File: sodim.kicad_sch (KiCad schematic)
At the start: 1 part, among them J1 ddr4-sodimm-edge-connector

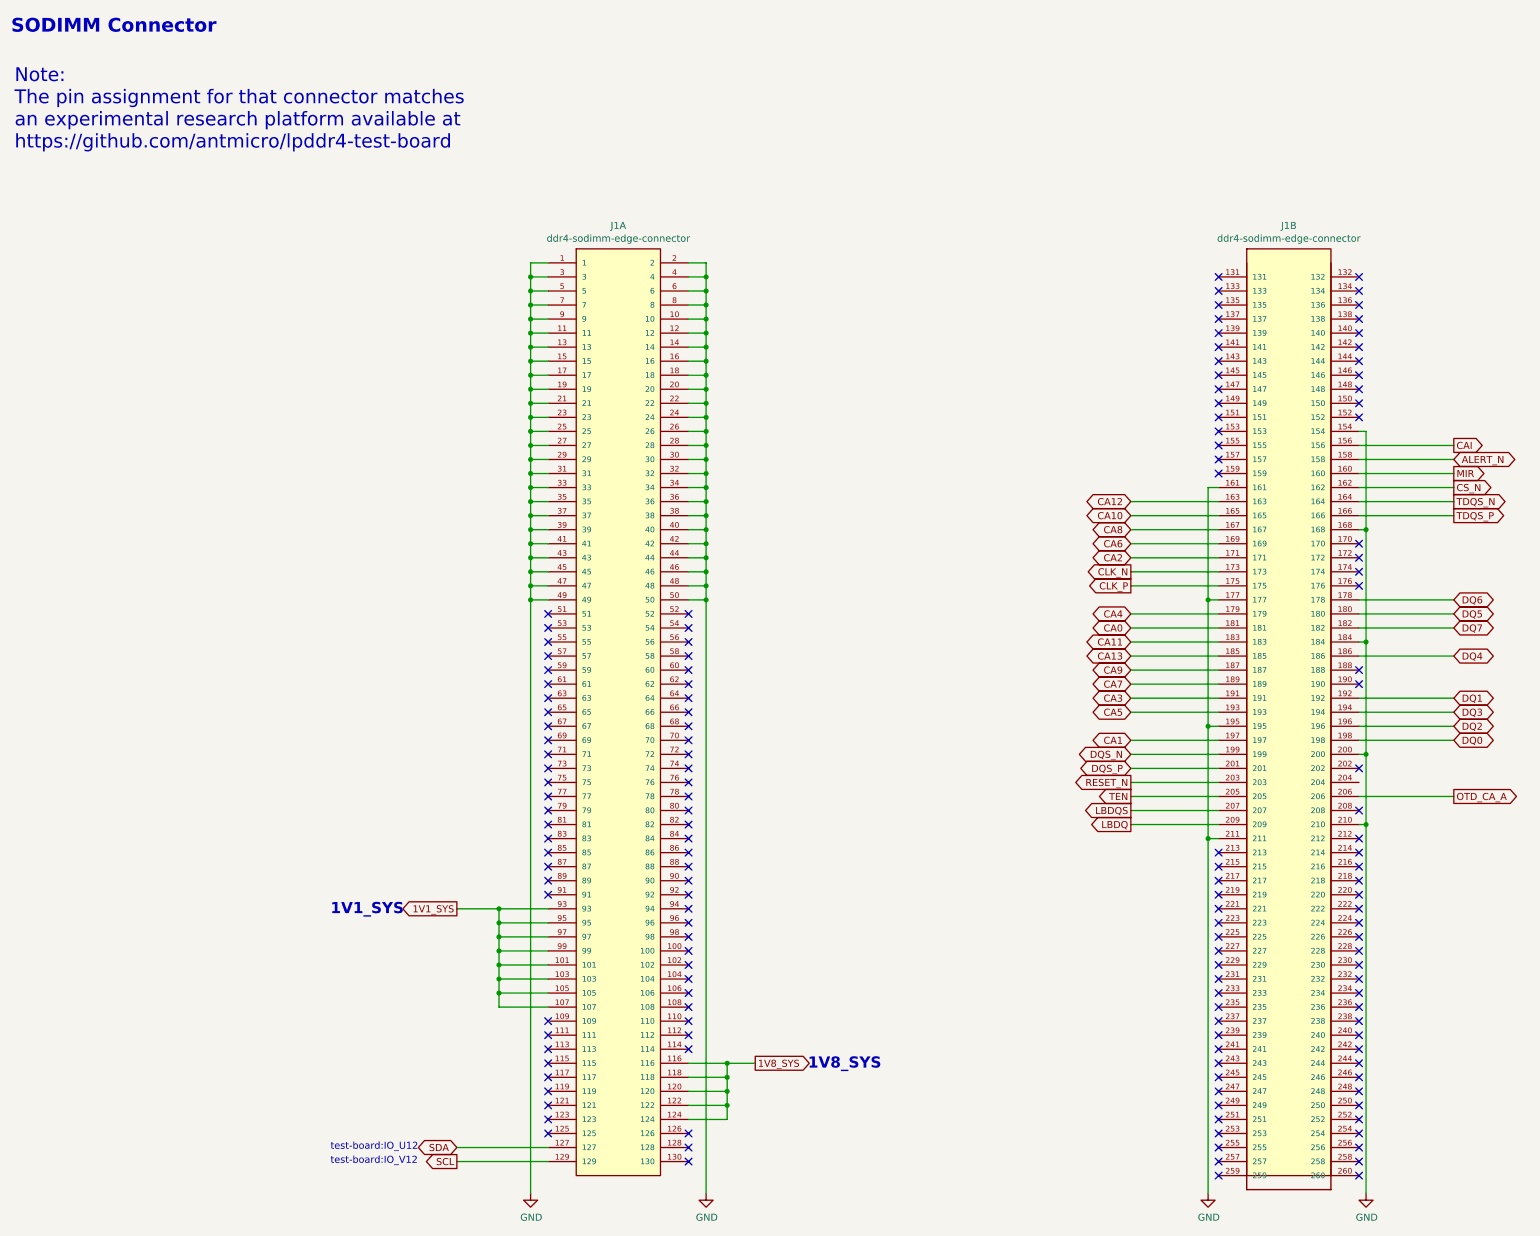
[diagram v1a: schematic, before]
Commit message: Introduce component standardization
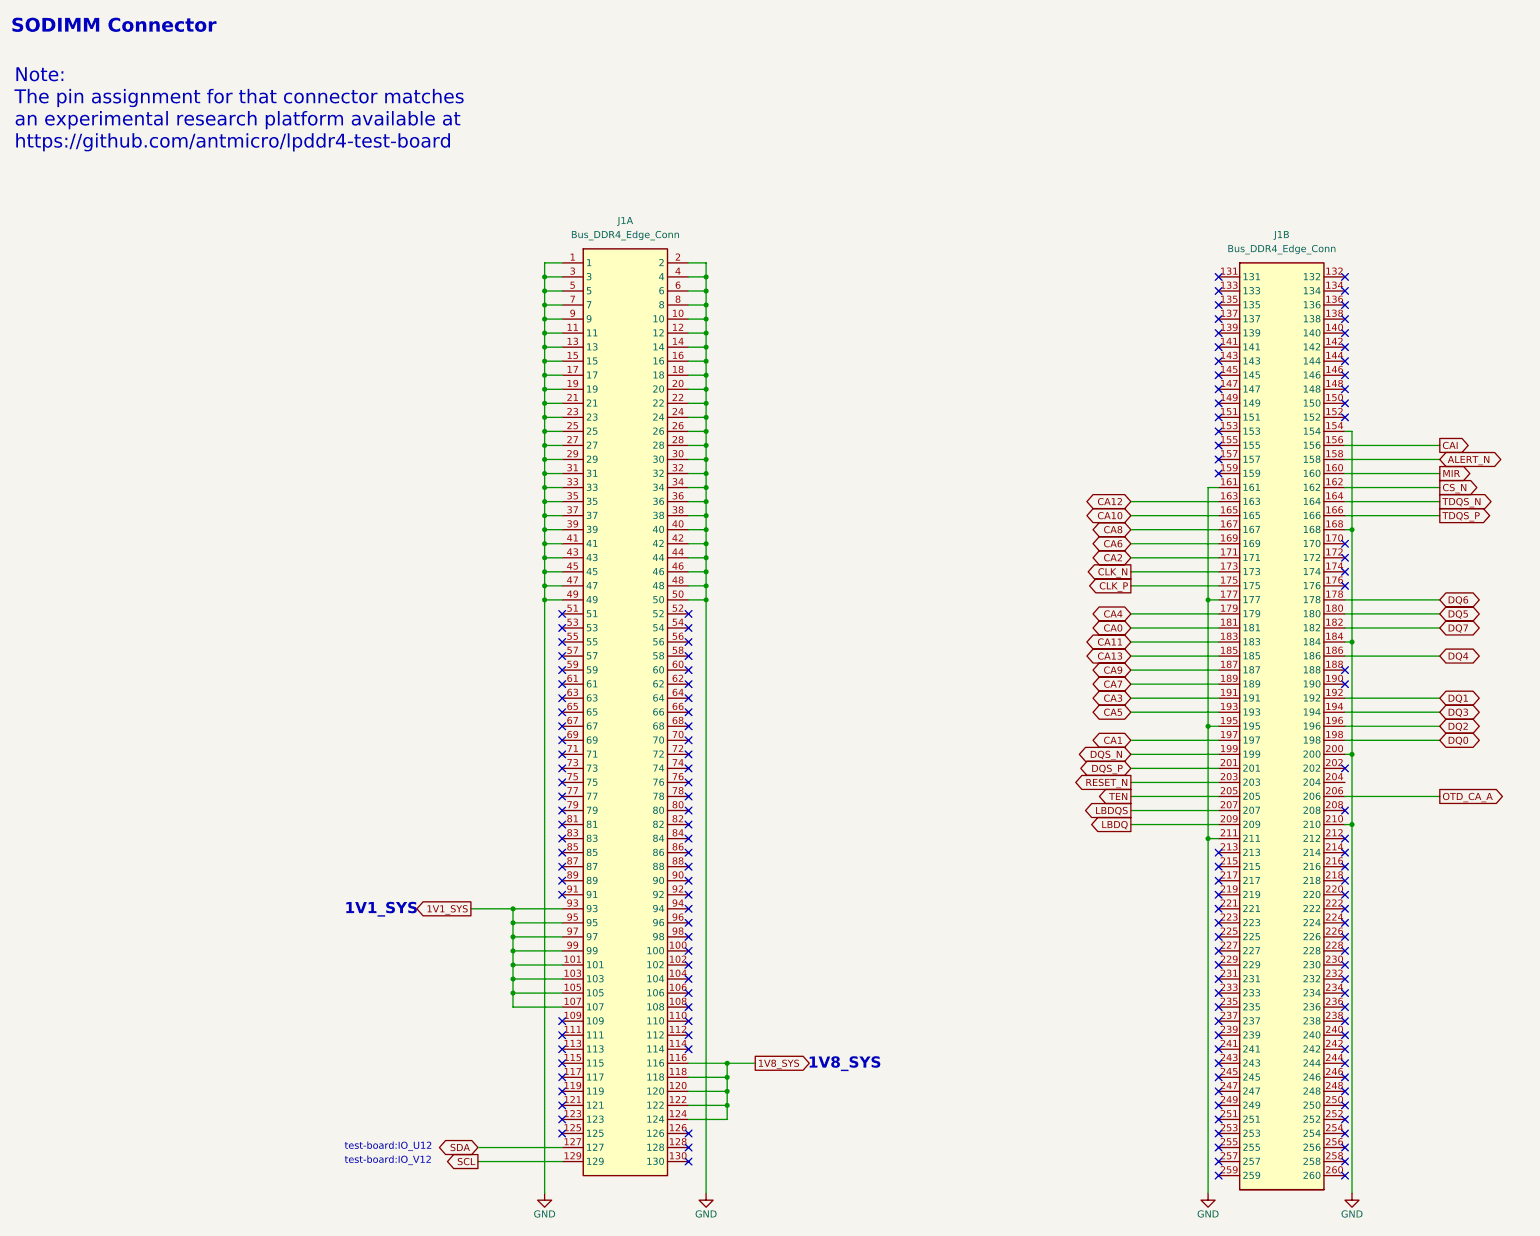
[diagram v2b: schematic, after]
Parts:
- J1: value ddr4-sodimm-edge-connector -> Bus_DDR4_Edge_Conn; footprint ddr5-testbed-footprints:SODIMM_DDR4_EDGE -> ddr5-testbed-footprints:Bus_DDR4_Conn_Edge; symbol ddr5-testbed:ddr4-sodimm-edge-connector -> ddr5-testbed:Bus_DDR4_Edge_Conn; Author (none) -> Antmicro; License (none) -> Apache-2.0
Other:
- moved on the sheet: J1A
